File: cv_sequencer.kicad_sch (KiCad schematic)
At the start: 69 parts, among them J1 4029_Connector_PicoBlade_4pos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, J2 4005_SWD_Header, J3 3086_Connector_Eurorack_Power, J4 3096_USBC_RA_SMD, SW1 RST, SW2 BOOTSEL, U1 3097_TFT_Display_SPI, U2 4002_RP2040, U3 4032_Adjustable_Reg_200mA_SOT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, U4 4032_Adjustable_Reg_200mA_SOT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

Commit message: some more routing
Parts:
- removed TP1: ENC_BTN, Shulltronics_Generics:TestPoint_Pad_D2.0mm, symbol Shulltronics_Sch_Symbols:TestPoint
- removed TP2: LCD/SD_SCK, Shulltronics_Generics:TestPoint_Pad_D2.0mm, symbol Shulltronics_Sch_Symbols:TestPoint
- removed TP3: SD_SDO, Shulltronics_Generics:TestPoint_Pad_D2.0mm, symbol Shulltronics_Sch_Symbols:TestPoint
- removed TP4: LCD/SD_SDI, Shulltronics_Generics:TestPoint_Pad_D2.0mm, symbol Shulltronics_Sch_Symbols:TestPoint
- removed TP5: LCD_CS, Shulltronics_Generics:TestPoint_Pad_D2.0mm, symbol Shulltronics_Sch_Symbols:TestPoint
- removed TP6: LCD_RST, Shulltronics_Generics:TestPoint_Pad_D2.0mm, symbol Shulltronics_Sch_Symbols:TestPoint
- removed TP7: LCD_DC, Shulltronics_Generics:TestPoint_Pad_D2.0mm, symbol Shulltronics_Sch_Symbols:TestPoint
- removed TP8: SD_CS, Shulltronics_Generics:TestPoint_Pad_D2.0mm, symbol Shulltronics_Sch_Symbols:TestPoint
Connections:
- net IO_TRIG0: now also U2.41 (GPIO29/ADC3); no longer U2.38 (GPIO26/ADC0)
- net IO_TRIG3: now also U2.38 (GPIO26/ADC0); no longer U2.41 (GPIO29/ADC3)
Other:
- note added: "Removed test points b.c. the header pads suffice"

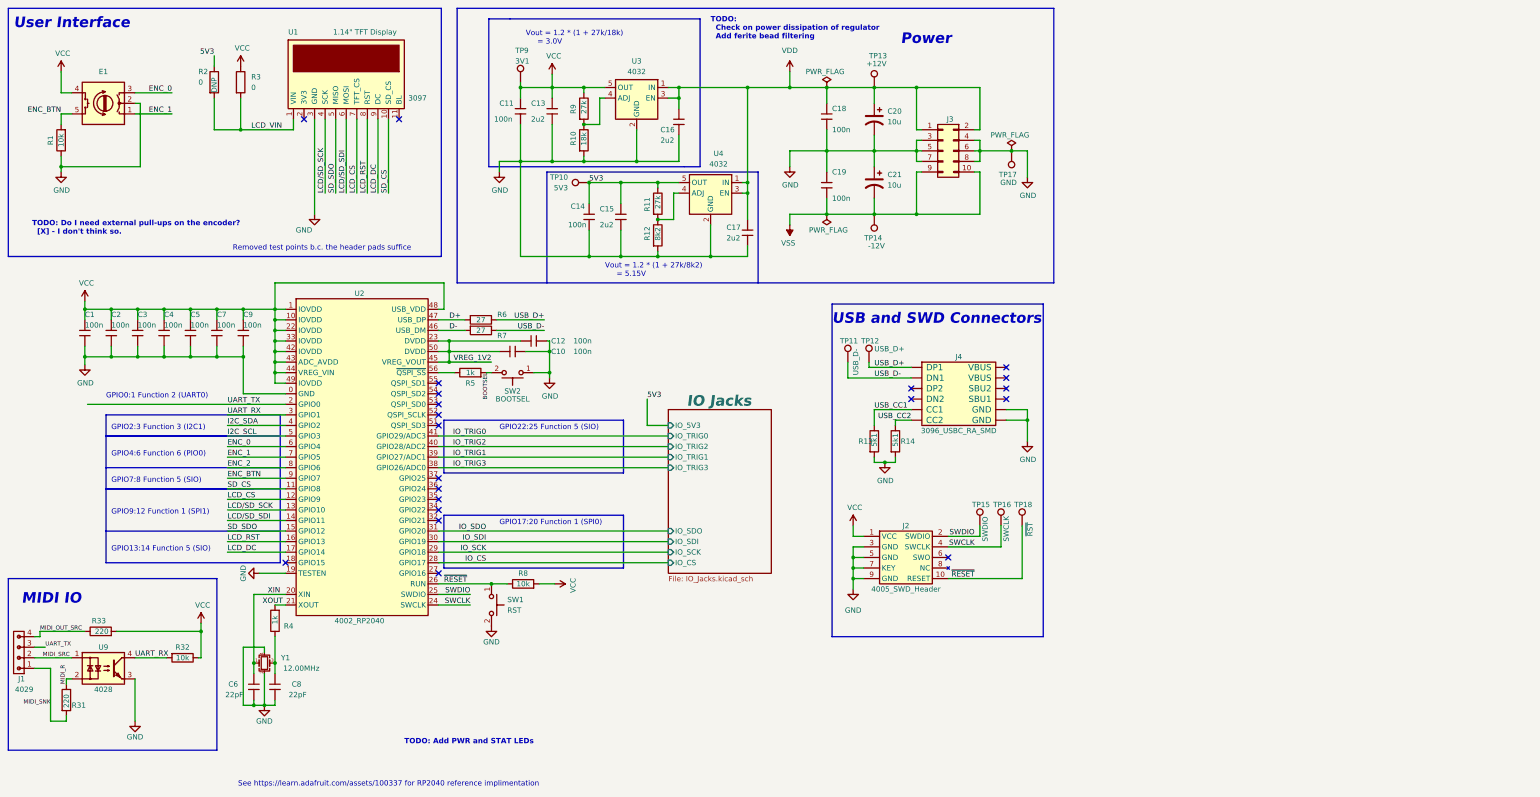
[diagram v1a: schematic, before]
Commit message: Added a few 0 ohm options, finished routing, ordered board!
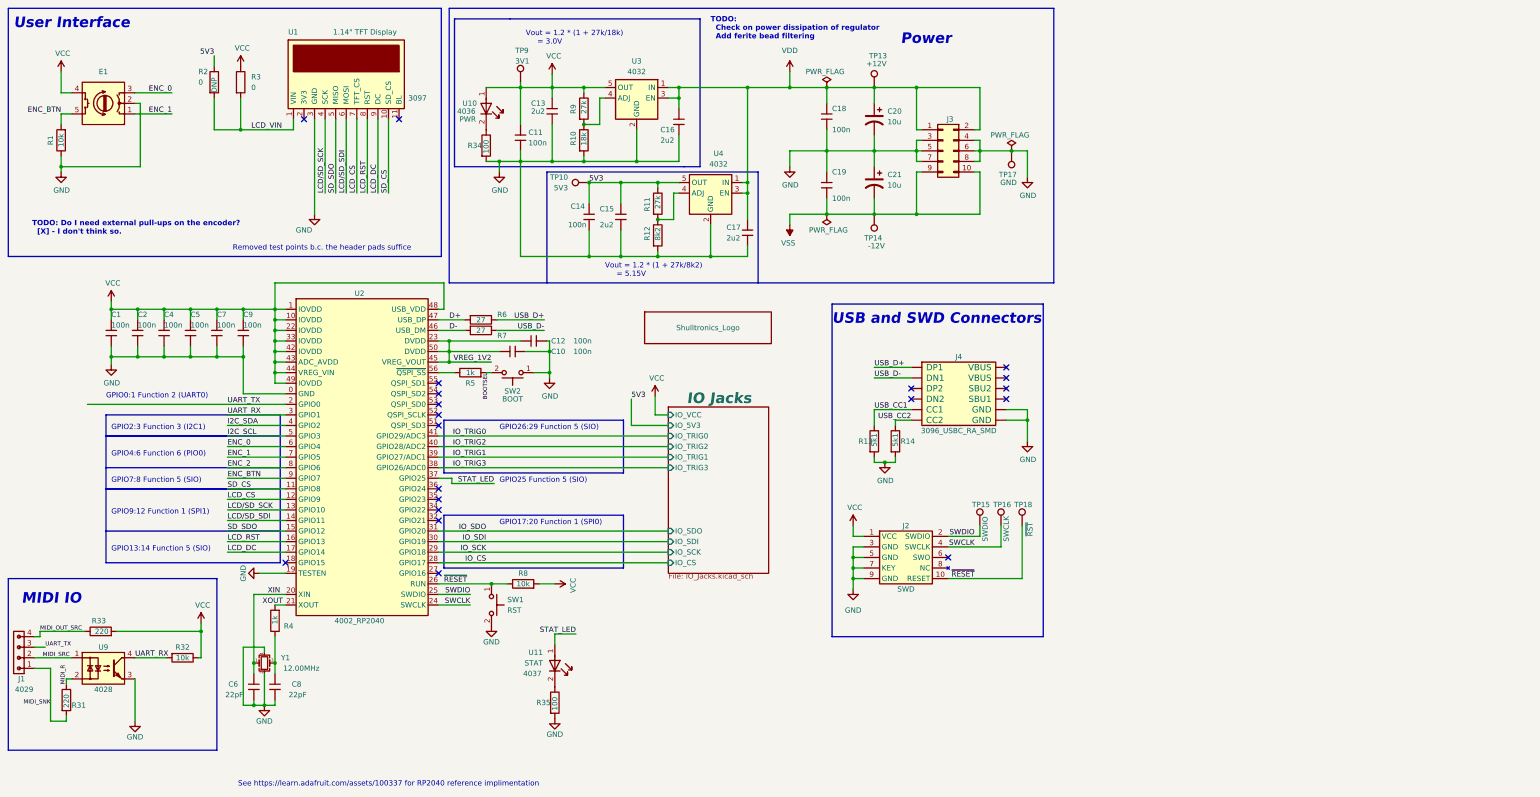
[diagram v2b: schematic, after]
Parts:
- removed C3: 3089_Capacitor_100n_16V_0402, Shulltronics_Generics:C_0402_HandSolder, symbol Shulltronics_Passives:3089_Capacitor_100n_16V_0402
- removed TP11: USB_D-, Shulltronics_Generics:TestPoint_Pad_D2.0mm, symbol Shulltronics_Sch_Symbols:TestPoint
- removed TP12: USB_D+, Shulltronics_Generics:TestPoint_Pad_D2.0mm, symbol Shulltronics_Sch_Symbols:TestPoint
- added L1: Shulltronics_Logo, Shulltronics_Generics:Shulltronics_Logo, symbol Shulltronics_Sch_Symbols:Shulltronics_Logo
- added R34, R35: 4038_Resistor_SMD_100_0.125W_1%, Shulltronics_Generics:RES-0402, symbol Shulltronics_Passives:4038_Resistor_SMD_100_0.125W_1%
- added U10: PWR, Shulltronics_Generics:LED_0402, symbol Shulltronics_Opto:4036_LED_GRN_SMD
- added U11: STAT, Shulltronics_Generics:LED_0402, symbol Shulltronics_Opto:4037_LED_YLW_SMD
- J1: value 4029_Connector_PicoBlade_4pos_Vert_THT -> :MIDI_IO
- J2: value 4005_SWD_Header -> SWD
- SW2: value BOOTSEL -> BOOT
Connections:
- net GND: now also R34.2, R35.2
- net VCC: now also U10.1 (A)
- net STAT_LED: now reaches U2.37 (GPIO25)
- net STAT_LED: now also U11.1 (A)
- new net: R34.1, U10.2 (K)
- new net: R35.1, U11.2 (K)
- no-connect marks 21 -> 20
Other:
- sheet IO Jacks ports: added IO_VCC; removed none
- note added: "GPIO25 Function 5 (SIO)"
- note added: "GPIO26:29 Function 5 (SIO)"
- note removed: "GPIO22:25 Function 5 (SIO)"
- note removed: "TODO: Add PWR and STAT LEDs"
- moved on the sheet: C1, C11, C2

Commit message: Changes from a while ago
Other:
- note added: "( ) - Test microcontroller circuitry (x) - uC powers on and executes code! :) ( ) - Add external Flash chip! ( ) - Add second set of USB signal so connector can be flipped! ( ) - Test all peripherals and analog circuitry ( ) - Create BOM Script that auto updates stock from distributors"
- note added: "Notes for revisions"

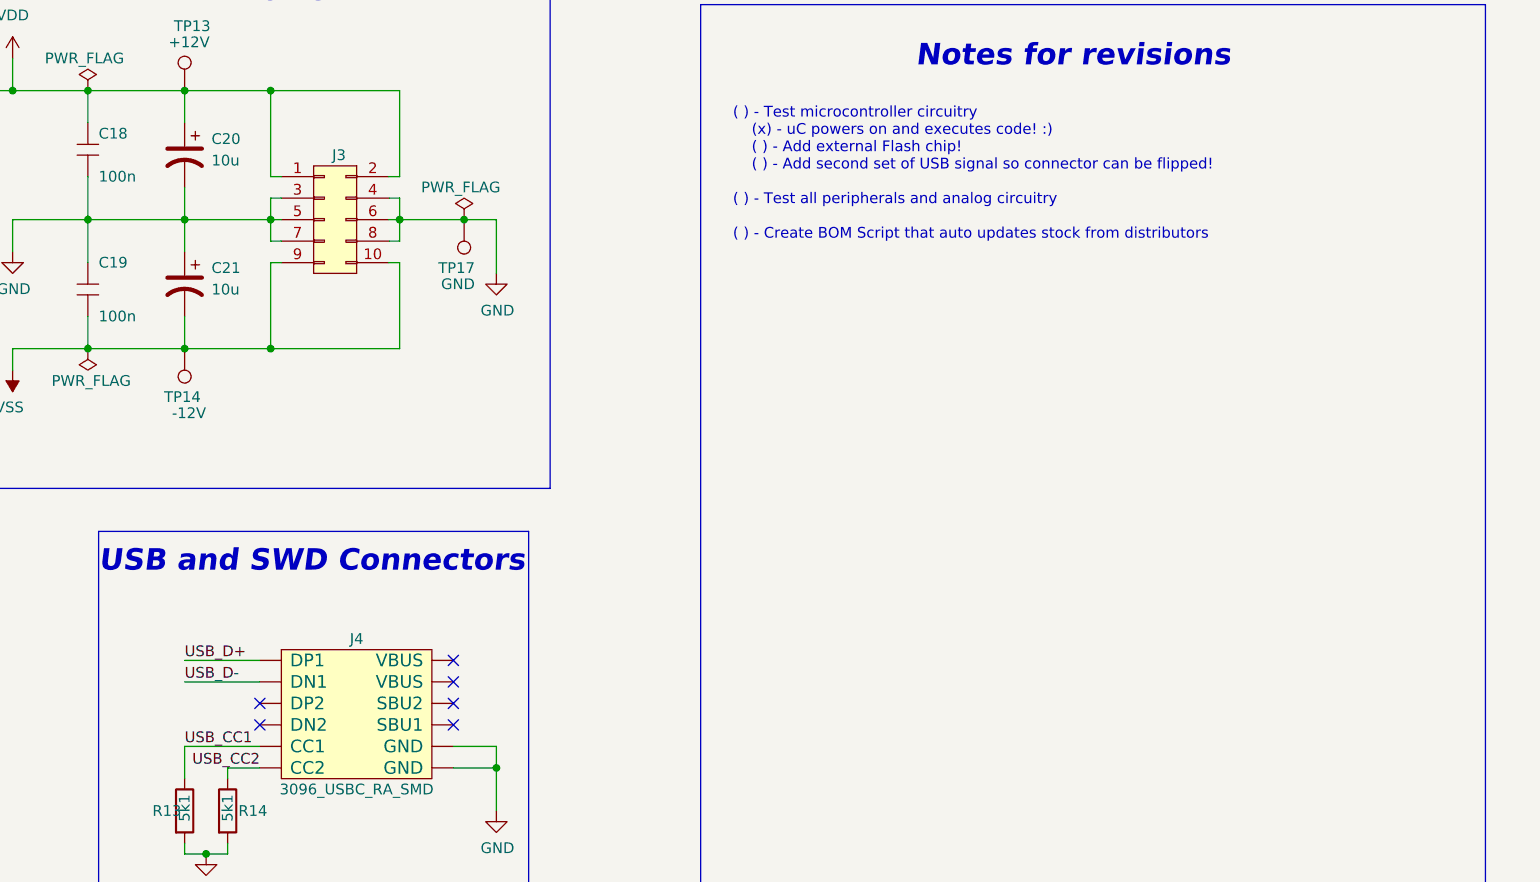
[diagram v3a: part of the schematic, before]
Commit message: Added USB other-side connections to schematic
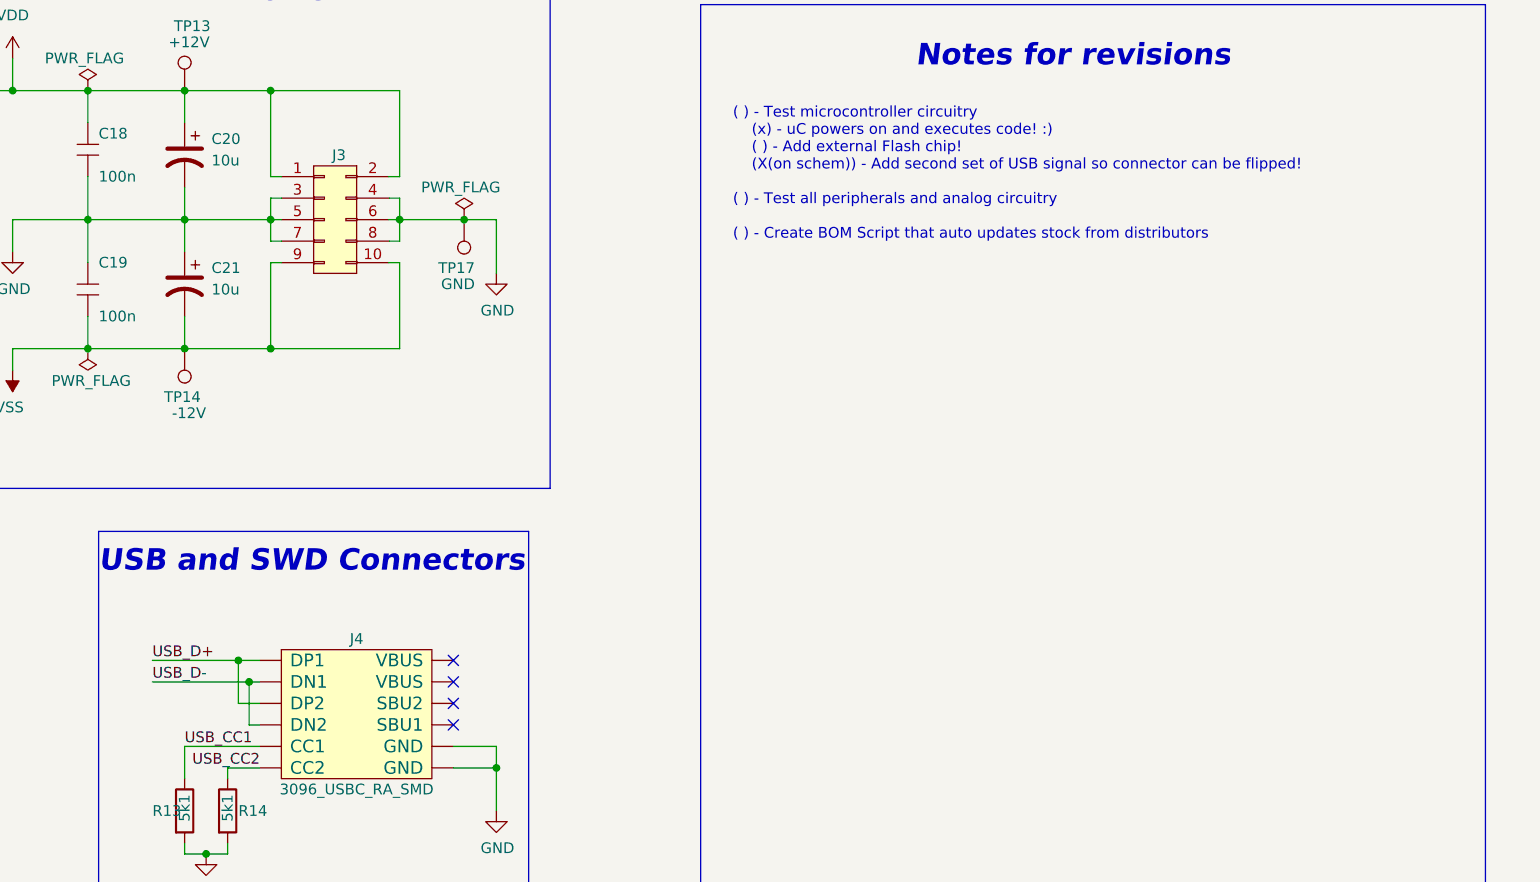
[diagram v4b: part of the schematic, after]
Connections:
- net USB_D+: now also J4.B6 (DP2)
- net USB_D-: now also J4.B7 (DN2)
- no-connect marks 20 -> 18
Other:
- note added: "( ) - Test microcontroller circuitry (x) - uC powers on and executes code! :) ( ) - Add external Flash chip! (X(on schem)) - Add second set of USB signal so connector can be flipped! ( ) - Test all peripherals and analog circuitry ( ) - Create BOM Script that auto updates stock from distributors"
- note removed: "( ) - Test microcontroller circuitry (x) - uC powers on and executes code! :) ( ) - Add external Flash chip! ( ) - Add second set of USB signal so connector can be flipped! ( ) - Test all peripherals and analog circuitry ( ) - Create BOM Script that auto updates stock from distributors"
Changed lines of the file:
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@@
     (effects (font (size 1.27 1.27)) (justify right bottom))
   )
-  (label "USB_D-" (at 222.25 102.87 0)
+  (label "USB_D-" (at 218.44 102.87 0)
     (effects (font (size 1.27 1.27)) (justify left bottom))
   )
@@
     (effects (font (size 1.27 1.27)) (justify left bottom))
   )
-  (label "USB_D+" (at 222.25 100.33 0)
+  (label "USB_D+" (at 218.44 100.33 0)
     (effects (font (size 1.27 1.27)) (justify left bottom))
   )

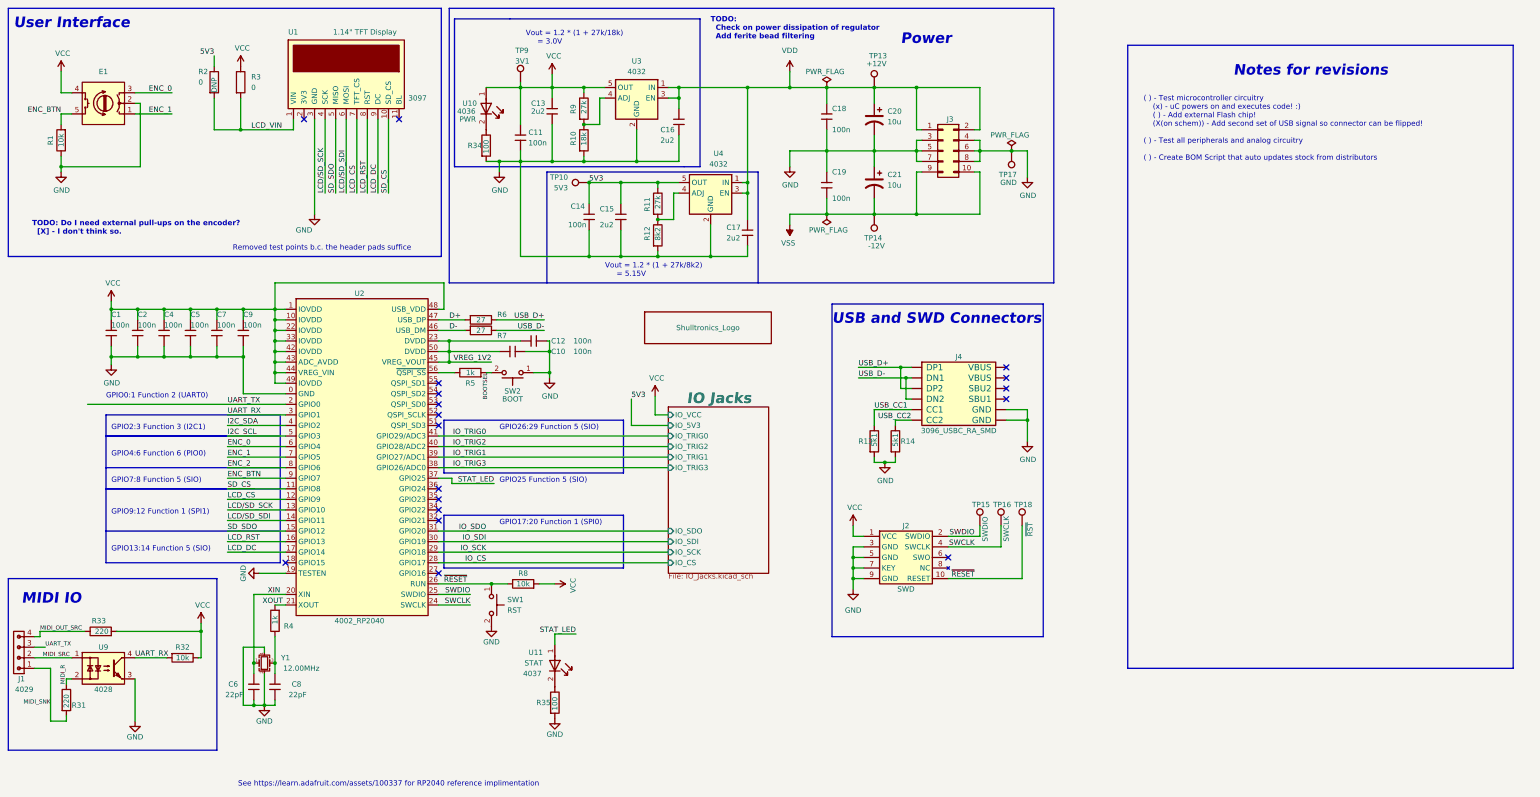
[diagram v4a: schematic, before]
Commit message: Added QSPI Flash to Schematic
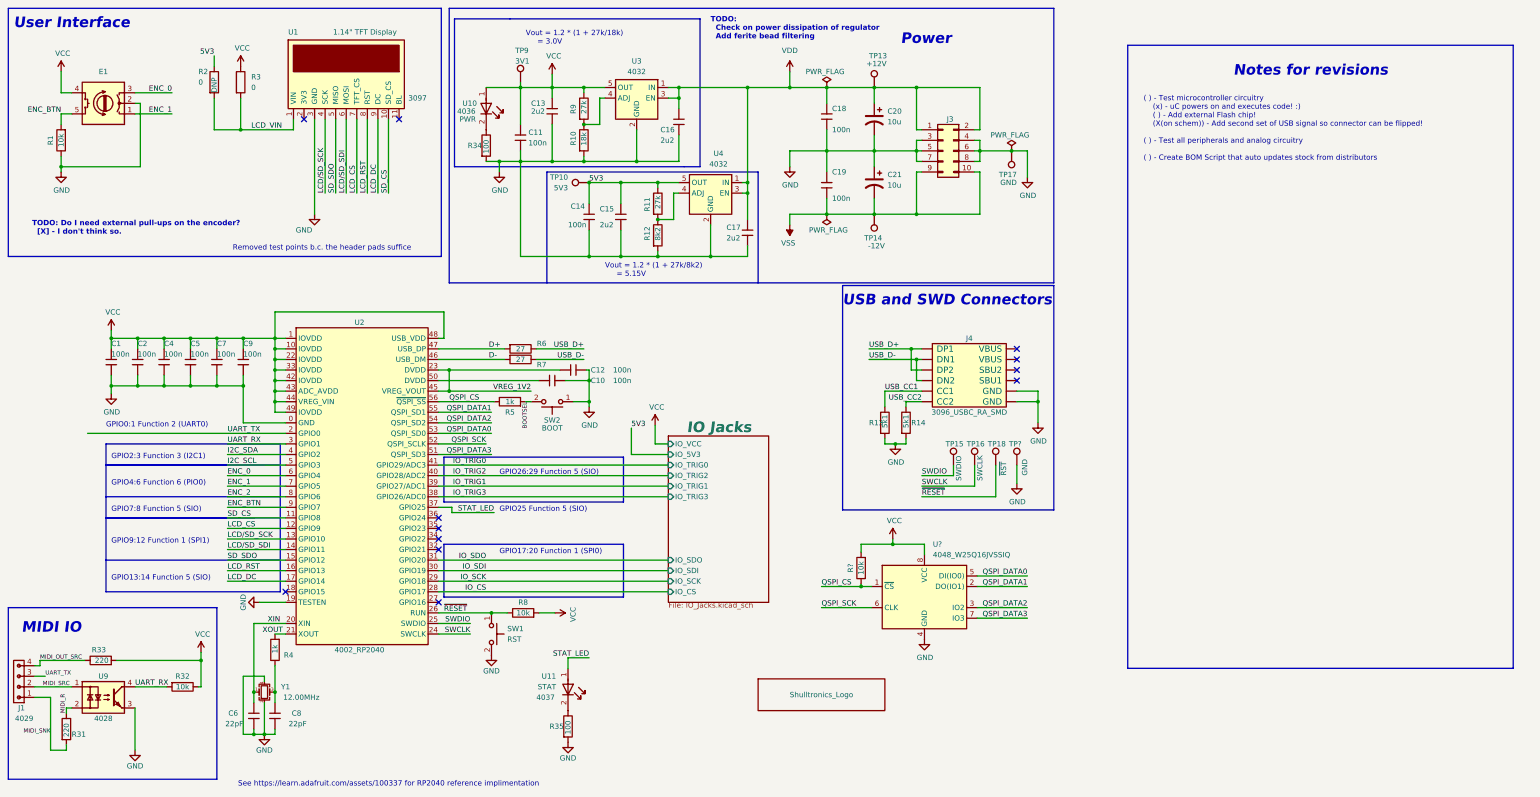
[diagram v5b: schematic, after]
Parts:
- removed J2: SWD, Shulltronics_Connectors:4005_SWD_Header, symbol Shulltronics_Connectors:4005_SWD_Header
- added R?: 4008_Resistor_SMD_10k_0.125W_1%, Shulltronics_Generics:RES-0402, symbol Shulltronics_Passives:4008_Resistor_SMD_10k_0.125W_1%
- added TP?: GND, Shulltronics_Generics:TestPoint_Pad_D2.0mm, symbol Shulltronics_Sch_Symbols:TestPoint
- added U?: 4048_W25Q16JVSSIQ, Shulltronics_Integrated_Circuits:4048_16Mb_Flash_SOIC8, symbol Shulltronics_ICs:4048_W25Q16JVSSIQ
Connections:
- net GND: now also TP?.1, U?.4 (GND)
- net VCC: now also R?.2, U?.8 (VCC)
- net VREG_1V2: no longer C10.1, U2.50 (DVDD)
- net QSPI_DATA3: now reaches U2.51 (QSPI_SD3)
- net QSPI_DATA3: now also U?.7 (IO3)
- net QSPI_SCK: now reaches U2.52 (QSPI_SCLK)
- net QSPI_SCK: now also U?.6 (CLK)
- net QSPI_DATA0: now reaches U2.53 (QSPI_SD0)
- net QSPI_DATA0: now also U?.5 (DI(IO0))
- net QSPI_DATA2: now reaches U2.54 (QSPI_SD2)
- net QSPI_DATA2: now also U?.3 (IO2)
- net QSPI_DATA1: now reaches U2.55 (QSPI_SD1)
- net QSPI_DATA1: now also U?.2 (DO(IO1))
- net QSPI_CS: now reaches R5.1, U2.56 (~{QSPI_SS})
- net QSPI_CS: now also R?.1, U?.1 (~{CS})
- new net: C10.1, U2.50 (DVDD)
- no-connect marks 18 -> 12
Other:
- moved on the sheet: C1, C10, C12, C2, C4, C5, C6, C7, C8, C9, J1, J4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
